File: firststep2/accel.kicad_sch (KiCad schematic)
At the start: 23 parts, among them J1 Conn_01x02, J2 Conn_01x03_Male, U1 LM317_TO-220, U2 TL431LP, U3 LM358

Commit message: firststep2
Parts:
- removed D1: SP0502BAHT, Package_TO_SOT_SMD:SOT-23, symbol Power_Protection:SP0502BAHT
- removed J1: Conn_01x02, Connector_Wago:Wago_734-162_1x02_P3.50mm_Horizontal, symbol Connector_Generic:Conn_01x02
- added D1: D_Zener, symbol Device:D_Zener
- added J2: Conn_01x03_Male, Connector:FanPinHeader_1x03_P2.54mm_Vertical, symbol Connector:Conn_01x03_Male
- added J3: Conn_5V, symbol Connector:Conn_01x01_Male
- added J5: Conn_GND, symbol Connector:Conn_01x01_Male
- added J6: Arduino_A6, symbol Connector:Conn_01x01_Male
- added J8: Arduino_A7, symbol Connector:Conn_01x01_Male
- C2: value 0,47u -> (none); footprint Capacitor_THT:C_Disc_D3.0mm_W2.0mm_P2.50mm -> (none)
- C3, C4: footprint Capacitor_THT:C_Disc_D3.0mm_W2.0mm_P2.50mm -> Capacitor_THT:CP_Radial_D4.0mm_P1.50mm
- C5: value 0,05 -> 0,01u
- C6: renamed from C?; value 1u -> 0.01u
- LA1: renamed from LA?; value BackLamp -> (none)
- R1: value 150 -> (none); footprint Resistor_THT:R_Axial_DIN0207_L6.3mm_D2.5mm_P7.62mm_Horizontal -> (none)
- R2: value 470 -> (none); footprint Resistor_THT:R_Axial_DIN0207_L6.3mm_D2.5mm_P7.62mm_Horizontal -> (none)
- R4: value 820 -> (none); footprint Resistor_THT:R_Axial_DIN0207_L6.3mm_D2.5mm_P7.62mm_Horizontal -> (none)
- U3: value LM358 -> (none); footprint Package_DIP:DIP-8_W7.62mm -> (none)
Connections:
- net ADC6: now also J6.1 (Pin_1)
- net ADC7: now also J8.1 (Pin_1)
- net GND: now also D1.1 (K), J5.1 (Pin_1); no longer RV1.2, RV1.3
- net 5VDC: no longer names the net of C1.1, U1.3 (VI)
- net 5VDC: now also J3.1 (Pin_1)
- net opamp renamed amp
- net amp: now also D1.2 (A); no longer R1.2
- new net: J2.1 (Pin_1), R1.2
- new net: J2.2 (Pin_2), RV1.2, RV1.3
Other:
- moved on the sheet: R1, RV1

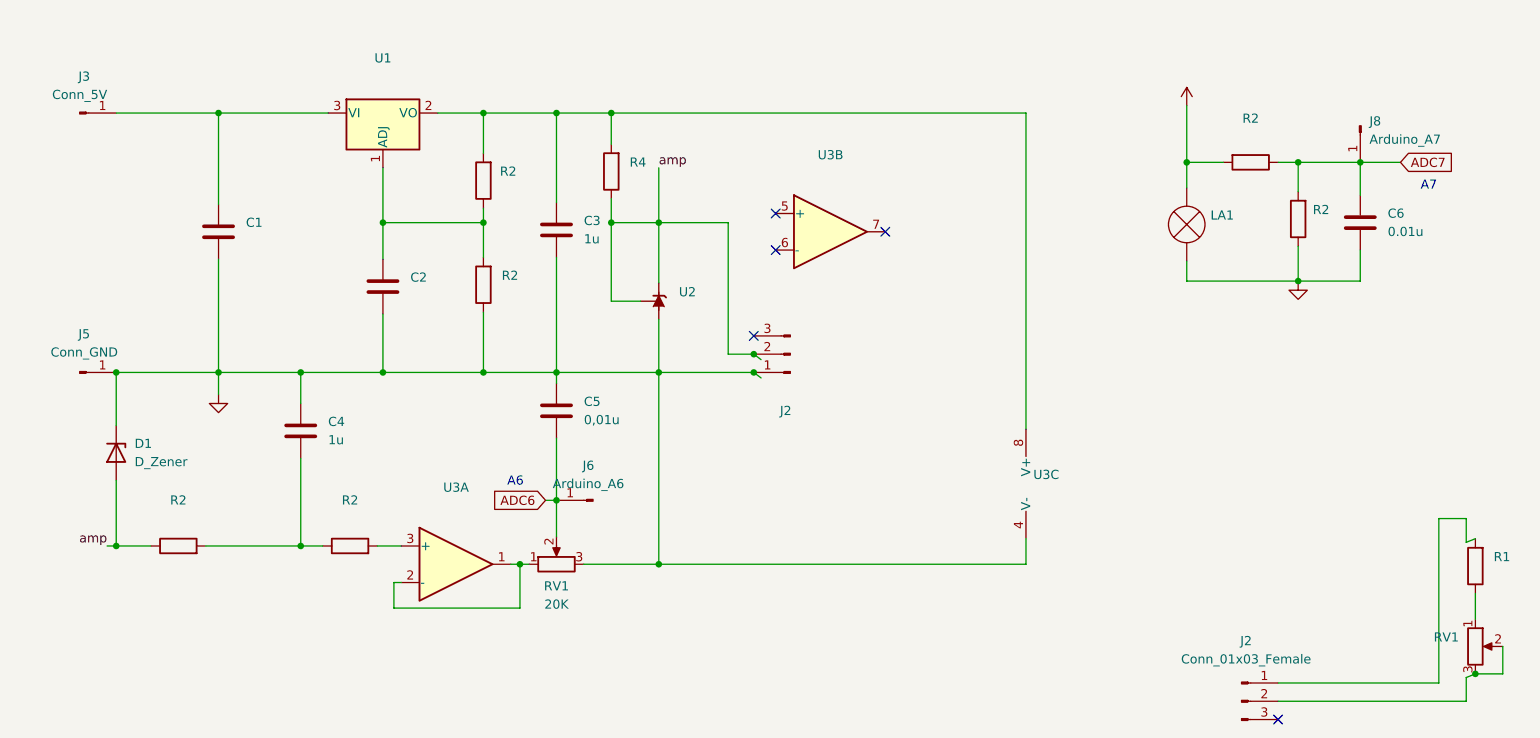
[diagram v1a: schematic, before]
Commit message: added atmega_logic, changed lm to tl
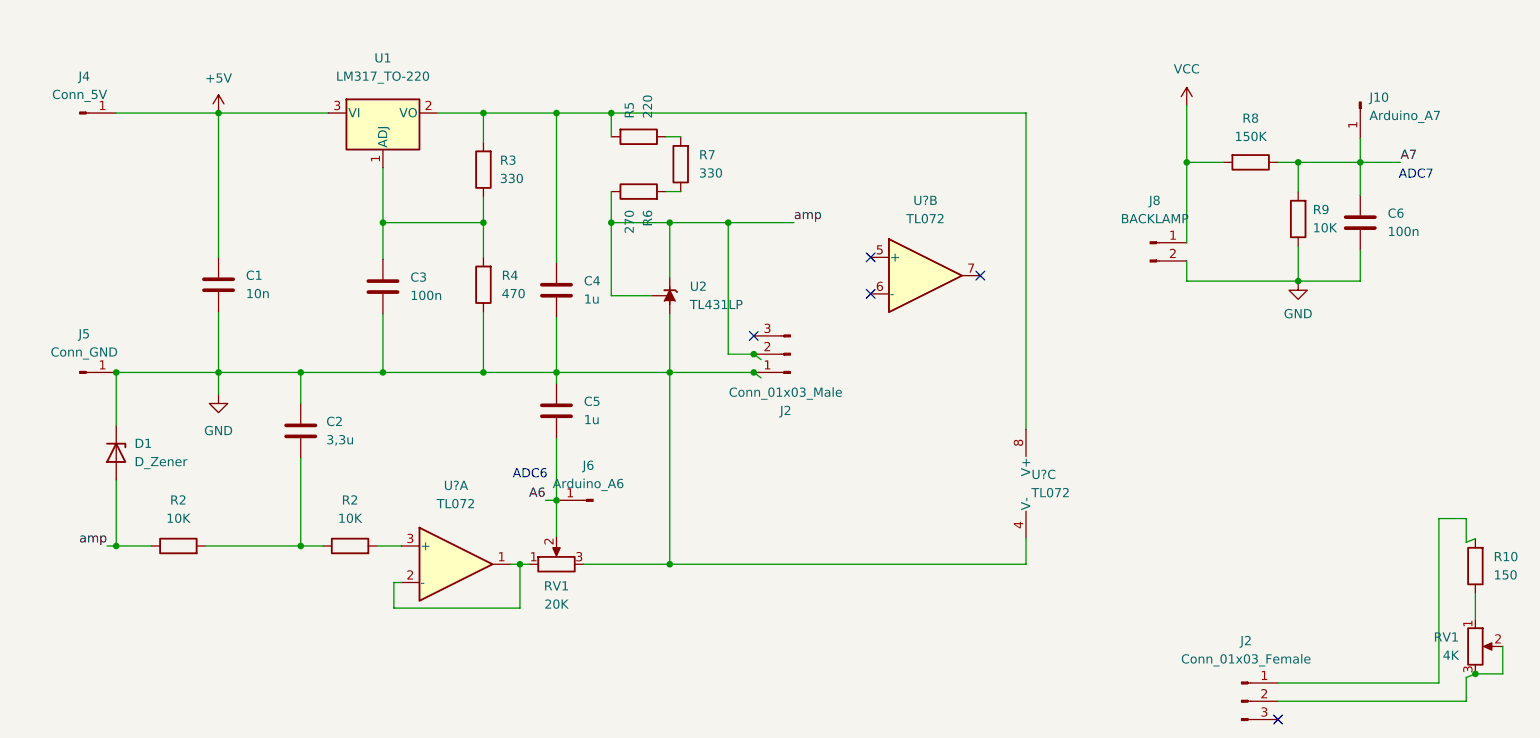
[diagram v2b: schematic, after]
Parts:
- removed LA1: (no value), symbol Device:Lamp
- removed U3: (no value), symbol Amplifier_Operational:LM358
- added J8: BACKLAMP, symbol Connector:Conn_01x02_Male
- added R6: 270, Resistor_THT:R_Axial_DIN0207_L6.3mm_D2.5mm_P7.62mm_Horizontal, symbol Device:R
- added R7: 330, Resistor_THT:R_Axial_DIN0207_L6.3mm_D2.5mm_P7.62mm_Horizontal, symbol Device:R
- added U? (x3): TL072, symbol Amplifier_Operational:TL072
- C1: value 10u -> 10n
- C2: renamed from C4; value 1u -> 3,3u
- C3: renamed from C2; value (none) -> 100n; footprint (none) -> Capacitor_THT:C_Disc_D3.0mm_W2.0mm_P2.50mm
- C5: value 0,01u -> 1u; footprint Capacitor_THT:C_Disc_D3.0mm_W1.6mm_P2.50mm -> Capacitor_THT:CP_Radial_D4.0mm_P1.50mm
- C6: value 0.01u -> 100n; footprint Capacitor_THT:C_Disc_D3.0mm_W2.0mm_P2.50mm -> Capacitor_THT:C_Disc_D5.0mm_W2.5mm_P2.50mm
- D1: footprint (none) -> Diode_THT:D_DO-34_SOD68_P7.62mm_Horizontal
- J10: renamed from J8; footprint (none) -> Connector_PinHeader_2.54mm:PinHeader_1x01_P2.54mm_Vertical
- J4: renamed from J3; footprint (none) -> Connector_PinHeader_2.54mm:PinHeader_1x01_P2.54mm_Vertical
- J5, J6: footprint (none) -> Connector_PinHeader_2.54mm:PinHeader_1x01_P2.54mm_Vertical
- R10: renamed from R1; value (none) -> 150
- R3: renamed from R2; footprint R_Axial_DIN0207_L6.3mm_D2.5mm_P7.62mm_Horizontal -> Resistor_THT:R_Axial_DIN0207_L6.3mm_D2.5mm_P7.62mm_Horizontal
- R4: renamed from R2; value (none) -> 470; footprint (none) -> Resistor_THT:R_Axial_DIN0207_L6.3mm_D2.5mm_P7.62mm_Horizontal
- R5: renamed from R4; value (none) -> 220; footprint (none) -> Resistor_THT:R_Axial_DIN0207_L6.3mm_D2.5mm_P7.62mm_Horizontal
- R8: renamed from R2; value 330 -> 150K; footprint R_Axial_DIN0207_L6.3mm_D2.5mm_P7.62mm_Horizontal -> Resistor_THT:R_Axial_DIN0207_L6.3mm_D2.5mm_P7.62mm_Horizontal
- R9: renamed from R2; value 330 -> 10K; footprint R_Axial_DIN0207_L6.3mm_D2.5mm_P7.62mm_Horizontal -> Resistor_THT:R_Axial_DIN0207_L6.3mm_D2.5mm_P7.62mm_Horizontal
- renumbered C3 to C4
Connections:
- net GND: now also C2.2, J8.2 (Pin_2), U?.4 (V-); no longer C2.1
- net amp: now also R6.1; no longer R5.1
- net +5V: now reaches C1.1, J4.1 (Pin_1), U1.3 (VI)
- net at C4.1, R3.2, R5.2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: now also U?.8 (V+)
- net at RV1.1: now also U?.1, U?.2 (-)
- net at R2.1, R2.2: now also C2.1; no longer C2.2
- net at R2.2: now also U?.3 (+)
- net +12V renamed VCC
- net VCC: now also J8.1 (Pin_1)
- net ADC6 renamed A6
- net ADC7 renamed A7
- new net: R6.2, R7.1
- new net: R5.1, R7.2
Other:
- note added: "ADC6"
- note added: "ADC7"
- note removed: "A6"
- note removed: "A7"
- moved on the sheet: C1, C2, C4, J10, R3, R5, U2

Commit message: update pcb
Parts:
- removed R6: 270, Resistor_THT:R_Axial_DIN0207_L6.3mm_D2.5mm_P7.62mm_Horizontal, symbol Device:R
- removed R7: 330, Resistor_THT:R_Axial_DIN0207_L6.3mm_D2.5mm_P7.62mm_Horizontal, symbol Device:R
- R5: value 220 -> 1K
- RV1: value R_Potentiometer -> 20K; footprint Potentiometer_THT:Potentiometer_ACP_CA9-V10_Vertical -> Potentiometer_THT:Potentiometer_Vishay_T73YP_Vertical
- U2: renamed from U?; footprint (none) -> Package_DIP:DIP-8_W7.62mm
- renumbered R8 to R6, R9 to R7, R10 to R8
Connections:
- net A6: now also C5.1; no longer C5.2
- net GND: now also C5.2, RV1.1; no longer C5.1, RV1.3
- net amp: now also R5.1
- net at U2.1, U2.2 (-): now also RV1.3; no longer RV1.1
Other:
- moved on the sheet: C5, RV1

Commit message: update pcb
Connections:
- net GND: now also D1.2 (A); no longer D1.1 (K)
- net amp: now also D1.1 (K); no longer D1.2 (A)
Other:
- moved on the sheet: D1
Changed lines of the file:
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@@
     (pin "2")
   )
-  (symbol (lib_id "Device:D_Zener") (at 45.72 106.68 270) (unit 1)
+  (symbol (lib_id "Device:D_Zener") (at 45.72 106.68 90) (unit 1)
     (in_bom yes) (on_board yes) (fields_autoplaced)
     (property "Reference" "D1" (id 0) (at 48.26 105.4099 90)
-      (effects (font (size 1.27 1.27)) (justify left))
+      (effects (font (size 1.27 1.27)) (justify right))
     )
     (property "Value" "D_Zener" (id 1) (at 48.26 107.9499 90)
-      (effects (font (size 1.27 1.27)) (justify left))
+      (effects (font (size 1.27 1.27)) (justify right))
     )
     (property "Footprint" "Diode_THT:D_DO-34_SOD68_P7.62mm_Horizontal" (id 2) (at 45.72 106.68 0)

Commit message: added NE555 50kHz gen
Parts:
- J8: footprint (none) -> Connector_PinHeader_2.54mm:PinHeader_1x02_P2.54mm_Vertical
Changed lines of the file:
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@@
     (property "Reference" "J8" (id 0) (at 190.119 71.628 0))
     (property "Value" "BACKLAMP" (id 1) (at 190.119 74.168 0))
-    (property "Footprint" "" (id 2) (at 189.484 77.47 0)
+    (property "Footprint" "Connector_PinHeader_2.54mm:PinHeader_1x02_P2.54mm_Vertical" (id 2) (at 189.484 77.47 0)
       (effects (font (size 1.27 1.27)) hide)
     )
